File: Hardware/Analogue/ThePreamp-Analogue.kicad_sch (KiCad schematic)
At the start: 36 parts, among them IC1 ULN2803CDWR, J1 To preamp, J10 Conn_01x04, J11 Conn_01x03, J14 Conn_01x03_Pin, J15 Switch & trigger outputs and 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, J2 From preamp, J3 Digital In, J4 Digital Pass Through, J5 Power In, J6 Power Out, J7 ADS1115, J8 Conn_01x04, J9 Conn_01x03, K1 Input 1, K2 Input 2, K3 Input 3, K4 Input 4, K5 Output Mute, K6 Trigger 1, K7 Trigger 2, K8 Input 5 (opt.), U1 MCP23008-E_SO

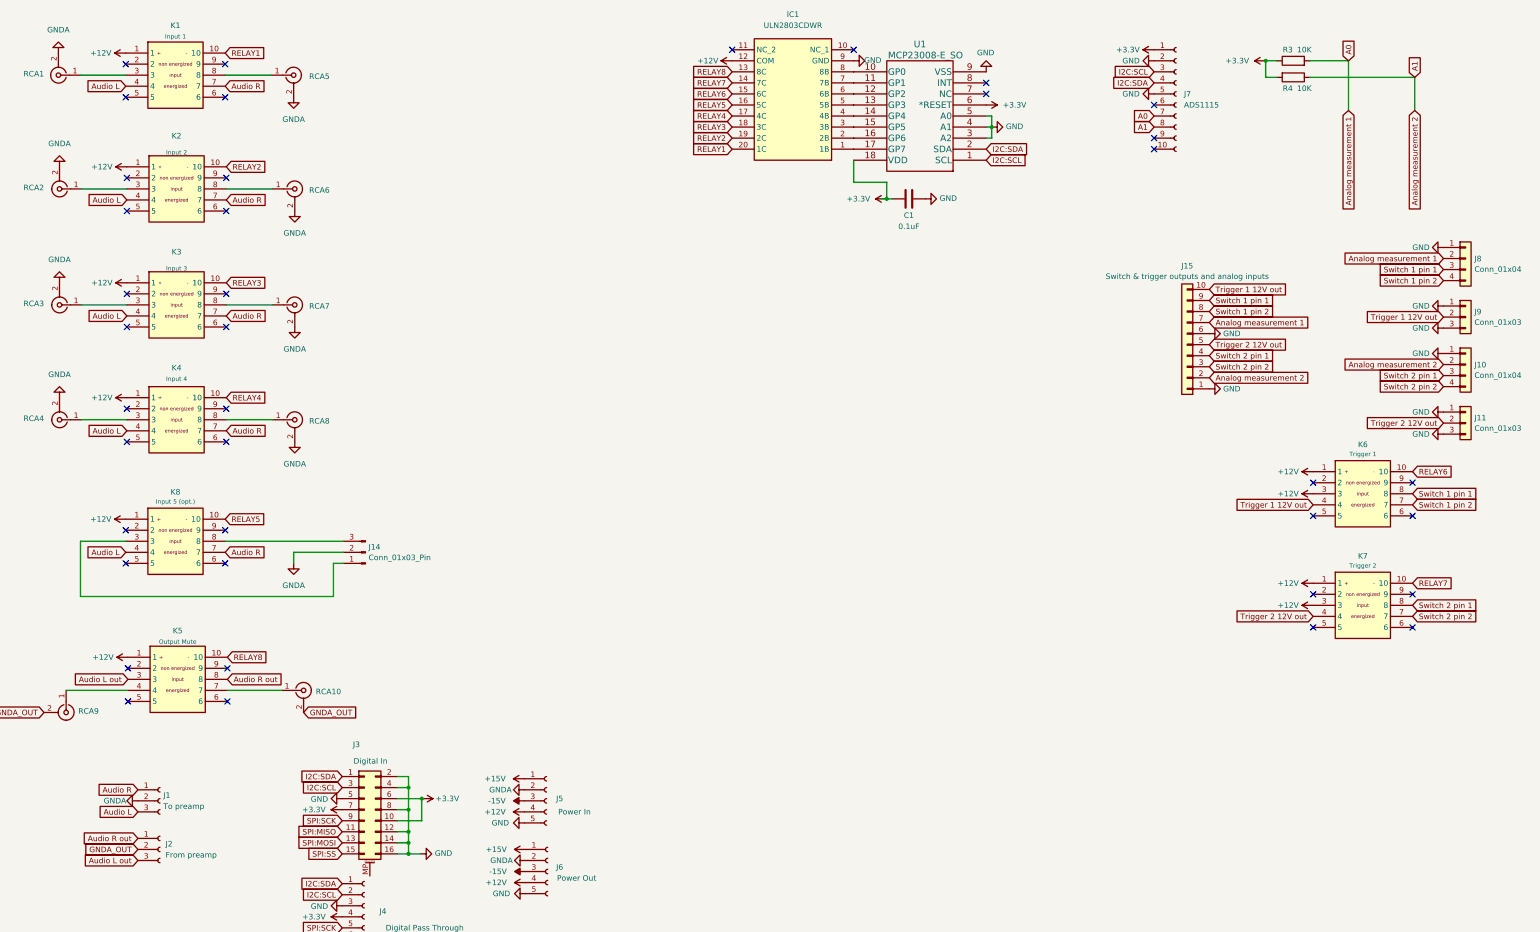
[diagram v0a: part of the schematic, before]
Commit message: Changed power connectors
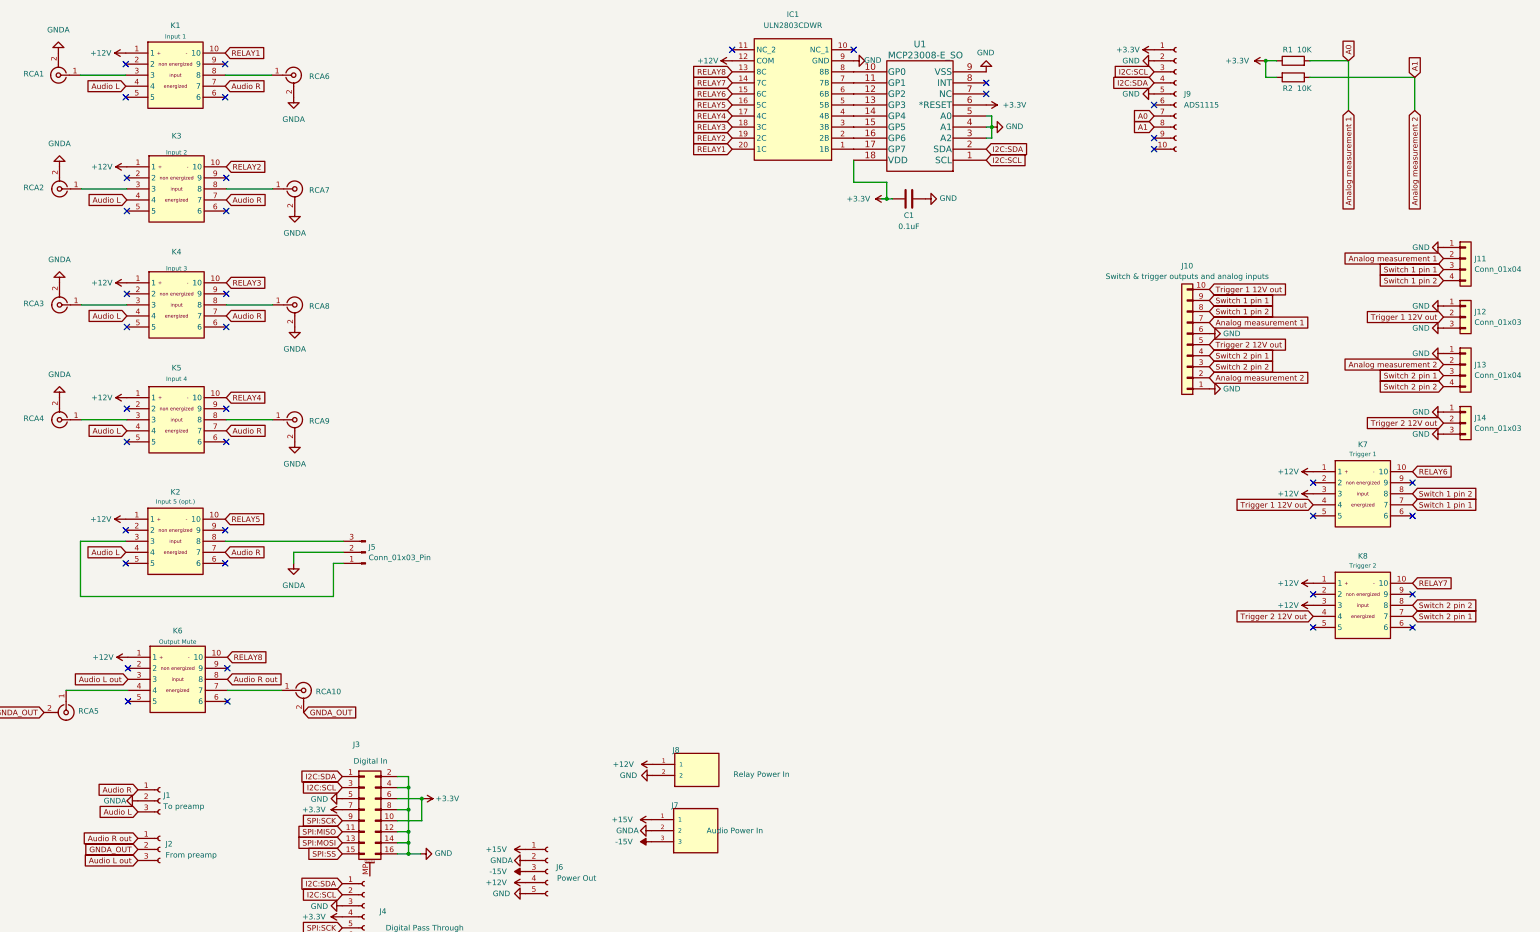
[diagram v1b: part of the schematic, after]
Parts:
- removed J5: Power In, Connector_JST:JST_XH_B5B-XH-A_1x05_P2.50mm_Vertical, symbol Connector:Conn_01x05_Female
- added J7: Audio Power In, THEPREAMP_POWER_CON:TBP01R2-508-03BK (VERT), symbol POWER_CONN_5_08:TBP01R2-508-03BK
- added J8: Relay Power In, THEPREAMP_POWER_CON:TBP01R2-508-02BK (VERT), symbol POWER_CONN_5_08:TBP01R2-508-02BK
- renumbered J15 to J10, J8 to J11, J9 to J12, J10 to J13, J11 to J14, J14 to J5, J7 to J9, K8 to K2, K2 to K3, K3 to K4, K4 to K5, K5 to K6, K6 to K7, K7 to K8, R3 to R1, R4 to R2, RCA9 to RCA5, RCA5 to RCA6, RCA6 to RCA7, RCA7 to RCA8, RCA8 to RCA9
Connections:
- net +12V: now also J8.1
- net +15V: now also J7.1
- net -15V: now also J7.3
- net GND: now also J8.2
- net GNDA: now also J7.2
- net Switch 1 pin 1: now also K7.7; no longer K7.8
- net Switch 1 pin 2: now also K7.8; no longer K7.7
- net Switch 2 pin 1: now also K8.7; no longer K8.8
- net Switch 2 pin 2: now also K8.8; no longer K8.7

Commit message: Ready for production
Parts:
- added J15: Conn_01x02_Pin, Connector_PinHeader_2.54mm:PinHeader_1x02_P2.54mm_Vertical, symbol Connector:Conn_01x02_Pin
- added R3, R4: 10K, Resistor_SMD:R_0805_2012Metric_Pad1.20x1.40mm_HandSolder, symbol Device:R
- J1, J2: footprint Connector_PinHeader_2.54mm:PinHeader_1x03_P2.54mm_Vertical -> PinSocket_1x03_P2.54mm_Vertical
- J4: footprint Connector_PinHeader_2.54mm:PinHeader_1x08_P2.54mm_Vertical -> Connector_PinSocket_2.54mm:PinSocket_1x08_P2.54mm_Vertical
- J6: footprint Connector_PinHeader_2.54mm:PinHeader_1x05_P2.54mm_Vertical -> PinSocket_1x05_P2.54mm_Vertical
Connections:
- net +3.3V: now also R3.2, R4.2
- net A3: now reaches J9.10 (Pin_10)
- net A3: now also J15.2 (Pin_2), R4.1
- net A2: now reaches J9.9 (Pin_9)
- net A2: now also J15.1 (Pin_1), R3.1
- no-connect marks 39 -> 38

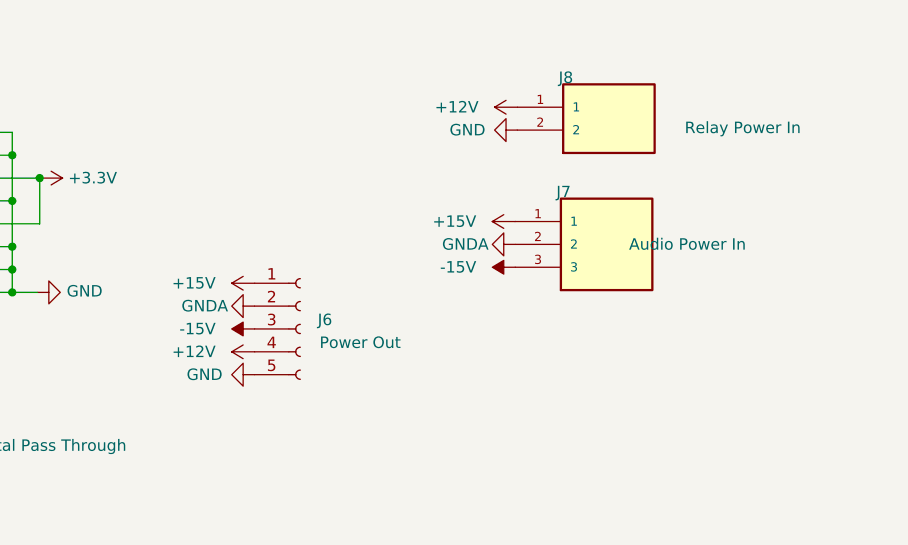
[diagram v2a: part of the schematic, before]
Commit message: Removed +/-15V connector from analog board
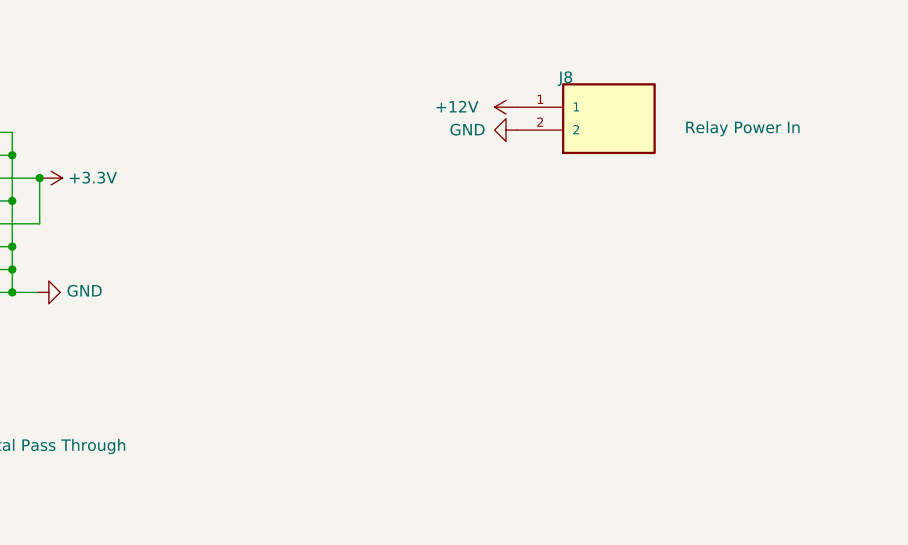
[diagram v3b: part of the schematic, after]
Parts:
- removed J6: Power Out, PinSocket_1x05_P2.54mm_Vertical, symbol Connector:Conn_01x05_Female
- removed J7: Audio Power In, THEPREAMP_POWER_CON:TBP01R2-508-03BK (VERT), symbol POWER_CONN_5_08:TBP01R2-508-03BK

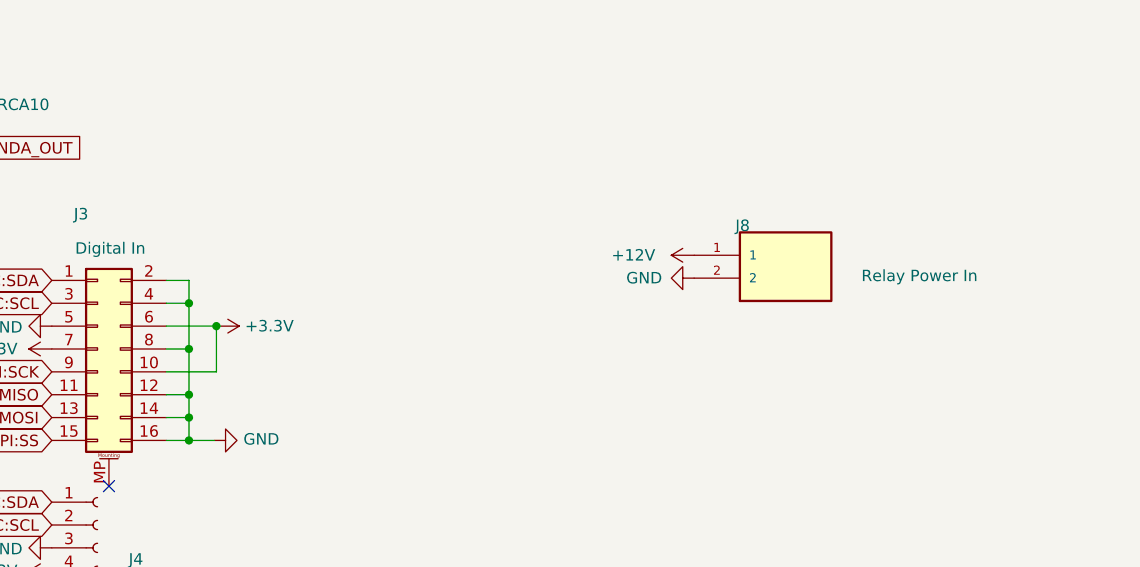
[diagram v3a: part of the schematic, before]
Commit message: Pcb dimensions
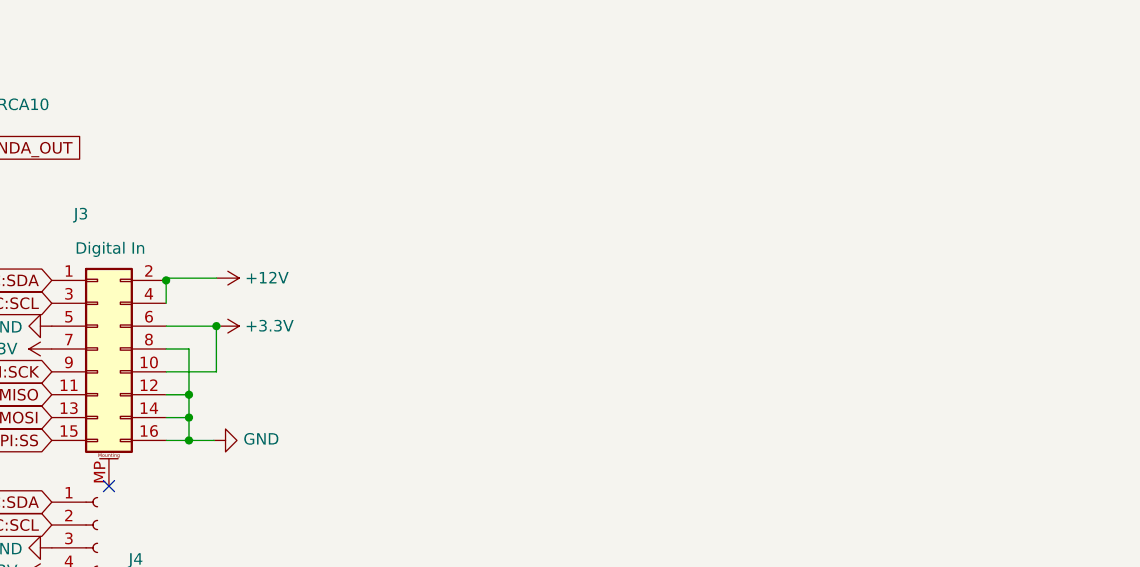
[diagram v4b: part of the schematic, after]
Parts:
- removed J8: Relay Power In, THEPREAMP_POWER_CON:TBP01R2-508-02BK (VERT), symbol POWER_CONN_5_08:TBP01R2-508-02BK
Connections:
- net +12V: now also J3.2 (Pin_2), J3.4 (Pin_4)
- net GND: no longer J3.2 (Pin_2), J3.4 (Pin_4)
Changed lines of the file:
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@@
 	)
 	(junction
-		(at 128.27 228.092)
-		(diameter 0)
-		(color 0 0 0 0)
-	)
-	(junction
 		(at 128.27 238.252)
 		(diameter 0)
@@
 	)
 	(junction
-		(at 128.27 223.012)
+		(at 125.73 220.472)
 		(diameter 0)
 		(color 0 0 0 0)
@@
 	(wire
 		(pts
-			(xy 128.27 220.472) (xy 128.27 223.012)
-		)
-		(stroke
-			(width 0)
-			(type default)
-		)
-	)
-	(wire
-		(pts
 			(xy 86.614 200.66) (xy 99.06 200.66)
 		)
@@
 	(wire
 		(pts
-			(xy 125.73 223.012) (xy 128.27 223.012)
+			(xy 125.73 223.012) (xy 125.73 220.472)
 		)
 		(stroke
@@
 	(wire
 		(pts
-			(xy 125.73 220.472) (xy 128.27 220.472)
+			(xy 125.73 235.712) (xy 128.27 235.712)
 		)
 		(stroke
@@
 	(wire
 		(pts
-			(xy 125.73 235.712) (xy 128.27 235.712)
+			(xy 128.27 238.252) (xy 125.73 238.252)
 		)
 		(stroke
@@
 	(wire
 		(pts
-			(xy 128.27 223.012) (xy 128.27 228.092)
+			(xy 335.28 59.69) (xy 344.17 59.69)
 		)
 		(stroke
@@
 	(wire
 		(pts
-			(xy 128.27 238.252) (xy 125.73 238.252)
+			(xy 327.66 55.88) (xy 325.374 55.88)
 		)
 		(stroke
@@
 	(wire
 		(pts
-			(xy 335.28 59.69) (xy 344.17 59.69)
+			(xy 230.632 78.74) (xy 230.632 83.82)
 		)
 		(stroke
@@
 	(wire
 		(pts
-			(xy 327.66 55.88) (xy 325.374 55.88)
+			(xy 125.73 228.092) (xy 128.27 228.092)
 		)
 		(stroke
@@
 	(wire
 		(pts
-			(xy 230.632 78.74) (xy 230.632 83.82)
+			(xy 354.33 71.12) (xy 354.33 67.31)
 		)
 		(stroke
@@
 	(wire
 		(pts
-			(xy 125.73 228.092) (xy 128.27 228.092)
+			(xy 125.73 225.552) (xy 131.318 225.552)
 		)
 		(stroke
@@
 	(wire
 		(pts
-			(xy 354.33 71.12) (xy 354.33 67.31)
+			(xy 86.36 138.43) (xy 97.028 138.43)
 		)
 		(stroke
@@
 	(wire
 		(pts
-			(xy 125.73 225.552) (xy 131.318 225.552)
+			(xy 262.382 68.58) (xy 262.382 71.12)
 		)
 		(stroke
@@
 	(wire
 		(pts
-			(xy 86.36 138.43) (xy 97.028 138.43)
+			(xy 344.17 59.69) (xy 344.17 71.12)
 		)
 		(stroke
@@
 	(wire
 		(pts
-			(xy 262.382 68.58) (xy 262.382 71.12)
+			(xy 339.09 71.12) (xy 339.09 55.88)
 		)
 		(stroke
@@
 	(wire
 		(pts
-			(xy 344.17 59.69) (xy 344.17 71.12)
+			(xy 230.632 83.82) (xy 238.252 83.82)
 		)
 		(stroke
@@
 	(wire
 		(pts
-			(xy 339.09 71.12) (xy 339.09 55.88)
+			(xy 125.73 220.472) (xy 125.73 220.218)
 		)
 		(stroke
@@
 	(wire
 		(pts
-			(xy 230.632 83.82) (xy 238.252 83.82)
+			(xy 238.252 83.82) (xy 238.252 87.63)
 		)
 		(stroke
@@
 	(wire
 		(pts
-			(xy 238.252 83.82) (xy 238.252 87.63)
+			(xy 125.73 220.218) (xy 131.318 220.218)
 		)
 		(stroke
@@
 	)
 	(symbol
-		(lib_id "power:+12V")
-		(at 184.404 217.678 90)
-		(unit 1)
-		(exclude_from_sim no)
-		(in_bom yes)
-		(on_board yes)
-		(dnp no)
-		(fields_autoplaced yes)
-		(property "Reference" "#PWR031"
-			(at 188.214 217.678 0)
-			(effects
-				(font
-					(size 1.27 1.27)
-				)
-				(hide yes)
-			)
-		)
-		(property "Value" "+12V"
-			(at 180.086 217.6779 90)
-			(effects
-				(font
-					(size 1.27 1.27)
-				)
-				(justify left)
-			)
-		)
-		(property "Footprint" ""
-			(at 184.404 217.678 0)
-			(effects
-				(font
-					(size 1.27 1.27)
-				)
-				(hide yes)
-			)
-		)
-		(property "Datasheet" ""
-			(at 184.404 217.678 0)
-			(effects
-				(font
-					(size 1.27 1.27)
-				)
-				(hide yes)
-			)
-		)
-		(property "Description" ""
-			(at 184.404 217.678 0)
-			(effects
-				(font
-					(size 1.27 1.27)
-				)
-				(hide yes)
-			)
-		)
-		(pin "1"
-		)
-		(instances
-			(project "ThePreamp-Analogue"
-				(path "/f6c644f4-3036-41a6-9e14-2c08c079c6cd"
-					(reference "#PWR031")
-					(unit 1)
-				)
-			)
-		)
-	)
-	(symbol
 		(lib_id "RCA ALI:RCA_Connector_ALI")
 		(at 101.854 59.182 0)
@@
 	)
 	(symbol
+		(lib_name "+12V_1")
+		(lib_id "power:+12V")
+		(at 131.318 220.218 270)
+		(unit 1)
+		(exclude_from_sim no)
+		(in_bom yes)
+		(on_board yes)
+		(dnp no)
+		(fields_autoplaced yes)
+		(property "Reference" "#PWR023"
+			(at 127.508 220.218 0)
+			(effects
+				(font
+					(size 1.27 1.27)
+				)
+				(hide yes)
+			)
+		)
+		(property "Value" "+12V"
+			(at 134.493 220.218 90)
+			(effects
+				(font
+					(size 1.27 1.27)
+				)
+				(justify left)
+			)
+		)
+		(property "Footprint" ""
+			(at 131.318 220.218 0)
+			(effects
+				(font
+					(size 1.27 1.27)
+				)
+				(hide yes)
+			)
+		)
+		(property "Datasheet" ""
+			(at 131.318 220.218 0)
+			(effects
+				(font
+					(size 1.27 1.27)
+				)
+				(hide yes)
+			)
+		)
+		(property "Description" "Power symbol creates a global label with name \"+12V\""
+			(at 131.318 220.218 0)
+			(effects
+				(font
+					(size 1.27 1.27)
+				)
+				(hide yes)
+			)
+		)
+		(pin "1"
+		)
+		(instances
+			(project "ThePreamp-Analogue"
+				(path "/f6c644f4-3036-41a6-9e14-2c08c079c6cd"
+					(reference "#PWR023")
+					(unit 1)
+				)
+			)
+		)
+	)
+	(symbol
 		(lib_id "Device:R")
 		(at 331.47 63.5 270)
@@
 	)
 	(symbol
-		(lib_id "POWER_CONN_5_08:TBP01R2-508-02BK")
-		(at 194.564 220.218 0)
-		(unit 1)
-		(exclude_from_sim no)
-		(in_bom yes)
-		(on_board yes)
-		(dnp no)
-		(property "Reference" "J8"
-			(at 188.976 215.138 0)
-			(effects
-				(font
-					(size 1.27 1.27)
-				)
-				(justify left bottom)
-			)
-		)
-		(property "Value" "Relay Power In"
-			(at 215.9 219.964 0)
-			(effects
-				(font
-					(size 1.27 1.27)
-				)
-				(justify right)
-			)
-		)
-		(property "Footprint" "THEPREAMP_POWER_CON:TBP01R2-508-02BK (VERT)"
-			(at 194.564 220.218 0)
-			(effects
-				(font
-					(size 1.27 1.27)
-				)
-				(justify left bottom)
-				(hide yes)
-			)
-		)
-		(property "Datasheet" "~"
-			(at 194.564 220.218 0)
-			(effects
-				(font
-					(size 1.27 1.27)
-				)
-				(justify left bottom)
-				(hide yes)
-			)
-		)
-		(property "Description" ""
-			(at 194.564 220.218 0)
-			(effects
-				(font
-					(size 1.27 1.27)
-				)
-				(hide yes)
-			)
-		)
-		(property "STANDARD" "Manufacturer Recommendations"
-			(at 194.564 220.218 0)
-			(effects
-				(font
-					(size 1.27 1.27)
-				)
-				(justify left bottom)
-				(hide yes)
-			)
-		)
-		(property "MANUFACTURER" "CUI"
-			(at 194.564 220.218 0)
-			(effects
-				(font
-					(size 1.27 1.27)
-				)
-				(justify left bottom)
-				(hide yes)
-			)
-		)
-		(pin "1"
-		)
-		(pin "2"
-		)
-		(instances
-			(project "ThePreamp-Analogue"
-				(path "/f6c644f4-3036-41a6-9e14-2c08c079c6cd"
-					(reference "J8")
-					(unit 1)
-				)
-			)
-		)
-	)
-	(symbol
 		(lib_id "RCA ALI:RCA_Connector_ALI")
 		(at 48.006 138.43 180)
@@
 					(unit 1)
 				)
-			)
-		)
-	)
-	(symbol
-		(lib_id "power:GND")
-		(at 184.404 220.218 270)
-		(unit 1)
-		(exclude_from_sim no)
-		(in_bom yes)
-		(on_board yes)
-		(dnp no)
-		(fields_autoplaced yes)
-		(property "Reference" "#PWR032"
-			(at 178.054 220.218 0)
-			(effects
-				(font
-					(size 1.27 1.27)
-				)
-				(hide yes)
-			)
-		)
-		(property "Value" "GND"
-			(at 180.848 220.2179 90)
-			(effects
-				(font
-					(size 1.27 1.27)
-				)
-				(justify right)
-			)
-		)
-		(property "Footprint" ""
-			(at 184.404 220.218 0)
-			(effects
-				(font
-					(size 1.27 1.27)
-				)
-				(hide yes)
-			)
-		)
-		(property "Datasheet" ""
-			(at 184.404 220.218 0)
-			(effects
-				(font
-					(size 1.27 1.27)
-				)
-				(hide yes)
-			)
-		)
-		(property "Description" ""
-			(at 184.404 220.218 0)
-			(effects
-				(font
-					(size 1.27 1.27)
-				)
-				(hide yes)
-			)
-		)
-		(pin "1"
-		)
-		(instances
-			(project "ThePreamp-Analogue"
-				(path "/f6c644f4-3036-41a6-9e14-2c08c079c6cd"
-					(reference "#PWR032")
-					(unit 1)
-				)
